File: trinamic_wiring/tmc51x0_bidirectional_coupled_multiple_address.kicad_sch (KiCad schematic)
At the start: 3 parts

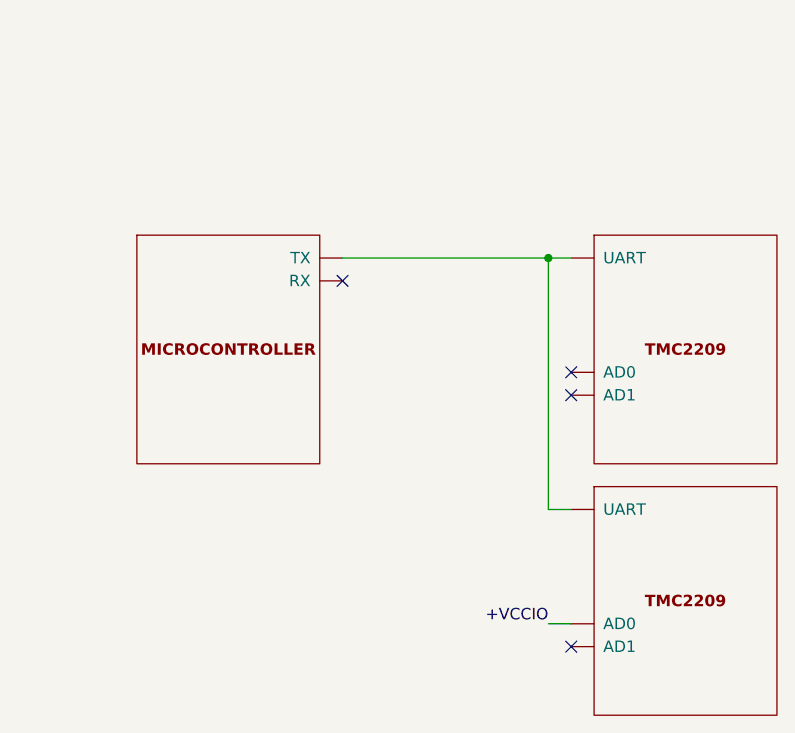
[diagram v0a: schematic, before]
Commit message: Add TMC51X0 files
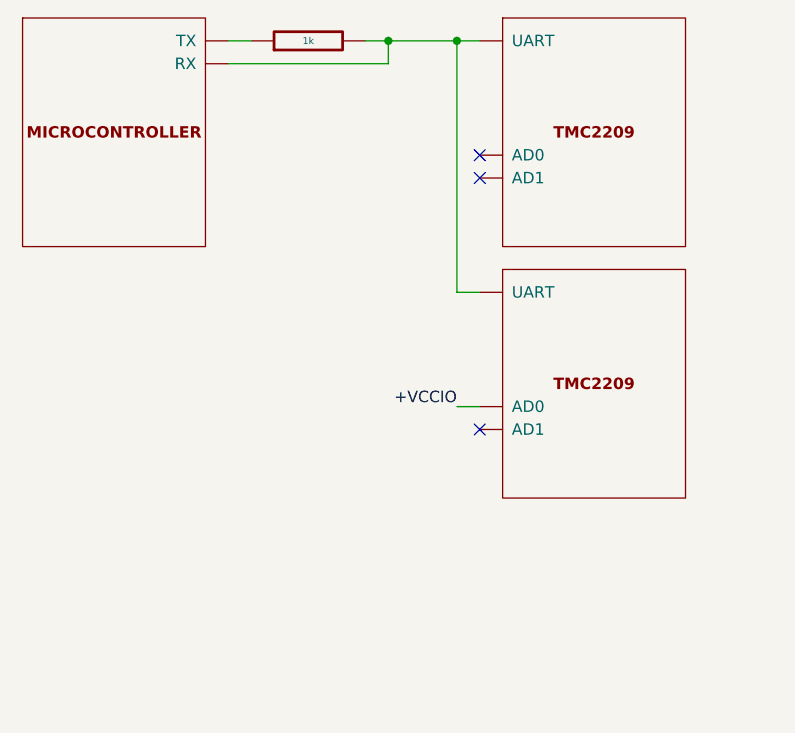
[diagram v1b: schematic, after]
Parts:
- removed MICROCONTROLLER3: DOC_MCU, symbol Janelia:DOC_MCU
- removed TMC4, TMC5: DOC_TMC2209, symbol Janelia:DOC_TMC2209
- added MICROCONTROLLER7: DOC_MCU, symbol Janelia:DOC_MCU
- added R4: 1k, Janelia:R_0402_1005Metric, symbol Janelia:R_1k_0402
- added TMC11, TMC12: DOC_TMC2209, symbol Janelia:DOC_TMC2209
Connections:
- net +VCCIO: now also TMC12.9 (AD0)
- new net: MICROCONTROLLER7.0 (RX), R4.2, TMC11.0 (UART), TMC12.0 (UART)
- new net: MICROCONTROLLER7.1 (TX), R4.1
- no-connect marks 4 -> 3
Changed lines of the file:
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@@
     (company "Janelia Research Campus")
   )
-  (junction (at 161.29 101.6) (diameter 0) (color 0 0 0 0)
+  (junction (at 151.13 77.47) (diameter 0) (color 0 0 0 0)
   )
-  (no_connect (at 163.83 116.84))
-  (no_connect (at 163.83 114.3))
-  (no_connect (at 138.43 104.14))
-  (no_connect (at 163.83 144.78))
-  (wire (pts (xy 161.29 101.6) (xy 161.29 129.54))
+  (junction (at 143.51 77.47) (diameter 0) (color 0 0 0 0)
+  )
+  (no_connect (at 153.67 120.65))
+  (no_connect (at 153.67 92.71))
+  (no_connect (at 153.67 90.17))
+  (wire (pts (xy 125.73 77.47) (xy 128.27 77.47))
     (stroke (width 0) (type default))
   )
-  (wire (pts (xy 138.43 101.6) (xy 161.29 101.6))
+  (wire (pts (xy 143.51 77.47) (xy 151.13 77.47))
     (stroke (width 0) (type default))
   )
-  (wire (pts (xy 161.29 142.24) (xy 163.83 142.24))
+  (wire (pts (xy 151.13 77.47) (xy 151.13 105.41))
     (stroke (width 0) (type default))
   )
-  (wire (pts (xy 161.29 129.54) (xy 163.83 129.54))
+  (wire (pts (xy 143.51 77.47) (xy 143.51 80.01))
     (stroke (width 0) (type default))
   )
-  (wire (pts (xy 161.29 101.6) (xy 163.83 101.6))
+  (wire (pts (xy 140.97 77.47) (xy 143.51 77.47))
     (stroke (width 0) (type default))
   )
-  (label "+VCCIO" (at 161.29 142.24 180) (fields_autoplaced)
+  (wire (pts (xy 151.13 77.47) (xy 153.67 77.47))
+    (stroke (width 0) (type default))
+  )
+  (wire (pts (xy 125.73 80.01) (xy 143.51 80.01))
+    (stroke (width 0) (type default))
+  )
+  (wire (pts (xy 151.13 105.41) (xy 153.67 105.41))
+    (stroke (width 0) (type default))
+  )
+  (wire (pts (xy 151.13 118.11) (xy 153.67 118.11))
+    (stroke (width 0) (type default))
+  )
+  (label "+VCCIO" (at 151.13 118.11 180) (fields_autoplaced)
     (effects (font (size 1.27 1.27)) (justify right bottom))
   )
-  (symbol (lib_id "Janelia:DOC_TMC2209") (at 176.53 139.7 0) (unit 1)
+  (symbol (lib_name "DOC_TMC2209_1") (lib_id "Janelia:DOC_TMC2209") (at 166.37 87.63 0) (unit 1)
     (in_bom yes) (on_board yes) (dnp no) (fields_autoplaced)
-    (property "Reference" "TMC5" (at 176.53 120.65 0)
+    (property "Reference" "TMC11" (at 166.37 68.58 0)
       (effects (font (size 1.27 1.27)) hide)
     )
-    (property "Value" "DOC_TMC2209" (at 176.53 125.73 0)
+    (property "Value" "DOC_TMC2209" (at 166.37 73.66 0)
       (effects (font (size 1.524 1.524)) hide)
     )
-    (property "Footprint" "" (at 173.99 166.37 0)
+    (property "Footprint" "" (at 163.83 114.3 0)
       (effects (font (size 1.524 1.524)) hide)
     )
-    (property "Datasheet" "" (at 176.53 139.7 0)
+    (property "Datasheet" "" (at 166.37 87.63 0)
       (effects (font (size 1.524 1.524)) hide)
     )
-    (property "Sim.Enable" "0" (at 176.53 123.19 0)
+    (property "Sim.Enable" "0" (at 166.37 71.12 0)
       (effects (font (size 1.27 1.27)) hide)
     )
@@
     (instances
       (project "trinamic_wiring"
-        (path "/e4144788-6304-493f-818e-5d881d3b7418/c8eda2b5-ab13-4033-82d9-875c9fcaf884/a2ce530e-f5b5-4e3e-9188-e4bc8f84c739"
-          (reference "TMC5") (unit 1)
+        (path "/e4144788-6304-493f-818e-5d881d3b7418/c8eda2b5-ab13-4033-82d9-875c9fcaf884/5f6f310d-167d-42a3-8815-1b623fe73dc8"
+          (reference "TMC11") (unit 1)
         )
-        (path "/e4144788-6304-493f-818e-5d881d3b7418/a161638e-a96f-4455-865a-1d7502675f43/a2ce530e-f5b5-4e3e-9188-e4bc8f84c739"
-          (reference "TMC6") (unit 1)
+        (path "/e4144788-6304-493f-818e-5d881d3b7418/a161638e-a96f-4455-865a-1d7502675f43/5f6f310d-167d-42a3-8815-1b623fe73dc8"
+          (reference "TMC11") (unit 1)
         )
       )
     )
   )
-  (symbol (lib_name "DOC_TMC2209_1") (lib_id "Janelia:DOC_TMC2209") (at 176.53 111.76 0) (unit 1)
+  (symbol (lib_id "Janelia:DOC_TMC2209") (at 166.37 115.57 0) (unit 1)
     (in_bom yes) (on_board yes) (dnp no) (fields_autoplaced)
-    (property "Reference" "TMC4" (at 176.53 92.71 0)
+    (property "Reference" "TMC12" (at 166.37 96.52 0)
       (effects (font (size 1.27 1.27)) hide)
     )
-    (property "Value" "DOC_TMC2209" (at 176.53 97.79 0)
+    (property "Value" "DOC_TMC2209" (at 166.37 101.6 0)
       (effects (font (size 1.524 1.524)) hide)
     )
-    (property "Footprint" "" (at 173.99 138.43 0)
+    (property "Footprint" "" (at 163.83 142.24 0)
       (effects (font (size 1.524 1.524)) hide)
     )
-    (property "Datasheet" "" (at 176.53 111.76 0)
+    (property "Datasheet" "" (at 166.37 115.57 0)
       (effects (font (size 1.524 1.524)) hide)
     )
-    (property "Sim.Enable" "0" (at 176.53 95.25 0)
+    (property "Sim.Enable" "0" (at 166.37 99.06 0)
       (effects (font (size 1.27 1.27)) hide)
     )
@@
     (instances
       (project "trinamic_wiring"
-        (path "/e4144788-6304-493f-818e-5d881d3b7418/c8eda2b5-ab13-4033-82d9-875c9fcaf884/a2ce530e-f5b5-4e3e-9188-e4bc8f84c739"
-          (reference "TMC4") (unit 1)
+        (path "/e4144788-6304-493f-818e-5d881d3b7418/c8eda2b5-ab13-4033-82d9-875c9fcaf884/5f6f310d-167d-42a3-8815-1b623fe73dc8"
+          (reference "TMC12") (unit 1)
         )
-        (path "/e4144788-6304-493f-818e-5d881d3b7418/a161638e-a96f-4455-865a-1d7502675f43/a2ce530e-f5b5-4e3e-9188-e4bc8f84c739"
-          (reference "TMC6") (unit 1)
+        (path "/e4144788-6304-493f-818e-5d881d3b7418/a161638e-a96f-4455-865a-1d7502675f43/5f6f310d-167d-42a3-8815-1b623fe73dc8"
+          (reference "TMC12") (unit 1)
         )
       )
     )
   )
-  (symbol (lib_id "Janelia:DOC_MCU") (at 125.73 111.76 0) (unit 1)
-    (in_bom yes) (on_board yes) (dnp no) (fields_autoplaced)
-    (property "Reference" "MICROCONTROLLER3" (at 125.73 92.71 0)
+  (symbol (lib_id "Janelia:R_1k_0402") (at 134.62 77.47 90) (unit 1)
+    (in_bom yes) (on_board yes) (dnp no)
+    (property "Reference" "R4" (at 134.62 76.2 0)
+      (effects (font (size 1.016 1.016)) (justify left) hide)
+    )
+    (property "Value" "1k" (at 134.62 77.47 90)
+      (effects (font (size 0.762 0.762)))
+    )
+    (property "Footprint" "Janelia:R_0402_1005Metric" (at 134.62 79.248 90)
+      (effects (font (size 0.762 0.762)) hide)
+    )
+    (property "Datasheet" "" (at 134.62 75.438 90)
+      (effects (font (size 0.762 0.762)))
+    )
+    (property "Vendor" "Digi-Key" (at 132.08 72.898 90)
+      (effects (font (size 1.524 1.524)) hide)
+    )
+    (property "Vendor Part Number" "311-1.00KLRCT-ND" (at 129.54 70.358 90)
+      (effects (font (size 1.524 1.524)) hide)
+    )
+    (property "Description" "RES SMD 1K OHM 1% 1/16W" (at 127 67.818 90)
+      (effects (font (size 1.524 1.524)) hide)
+    )
+    (property "Package" "0402" (at 134.62 77.47 0)
       (effects (font (size 1.27 1.27)) hide)
     )
-    (property "Value" "DOC_MCU" (at 125.73 97.79 0)
+    (property "Manufacturer" "YAGEO" (at 134.62 77.47 0)
+      (effects (font (size 1.27 1.27)) hide)
+    )
+    (property "Manufacturer Part Number" "RC0402FR-071KL" (at 134.62 77.47 0)
+      (effects (font (size 1.27 1.27)) hide)
+    )
+    (pin "1")
+    (pin "2")
+    (instances
+      (project "trinamic_wiring"
+        (path "/e4144788-6304-493f-818e-5d881d3b7418/c8eda2b5-ab13-4033-82d9-875c9fcaf884/5f6f310d-167d-42a3-8815-1b623fe73dc8"
+          (reference "R4") (unit 1)
+        )
+        (path "/e4144788-6304-493f-818e-5d881d3b7418/a161638e-a96f-4455-865a-1d7502675f43/5f6f310d-167d-42a3-8815-1b623fe73dc8"
+          (reference "R4") (unit 1)
+        )
+      )
+    )
+  )
+  (symbol (lib_id "Janelia:DOC_MCU") (at 113.03 87.63 0) (unit 1)
+    (in_bom yes) (on_board yes) (dnp no) (fields_autoplaced)
+    (property "Reference" "MICROCONTROLLER7" (at 113.03 68.58 0)
+      (effects (font (size 1.27 1.27)) hide)
+    )
+    (property "Value" "DOC_MCU" (at 113.03 73.66 0)
       (effects (font (size 1.524 1.524)) hide)
     )
-    (property "Footprint" "" (at 123.19 138.43 0)
+    (property "Footprint" "" (at 110.49 114.3 0)
       (effects (font (size 1.524 1.524)) hide)
     )
-    (property "Datasheet" "" (at 125.73 111.76 0)
+    (property "Datasheet" "" (at 113.03 87.63 0)
       (effects (font (size 1.524 1.524)) hide)
     )
-    (property "Sim.Enable" "0" (at 125.73 95.25 0)
+    (property "Sim.Enable" "0" (at 113.03 71.12 0)
       (effects (font (size 1.27 1.27)) hide)
     )
@@
     (instances
       (project "trinamic_wiring"
-        (path "/e4144788-6304-493f-818e-5d881d3b7418/c8eda2b5-ab13-4033-82d9-875c9fcaf884/a2ce530e-f5b5-4e3e-9188-e4bc8f84c739"
-          (reference "MICROCONTROLLER3") (unit 1)
+        (path "/e4144788-6304-493f-818e-5d881d3b7418/c8eda2b5-ab13-4033-82d9-875c9fcaf884/5f6f310d-167d-42a3-8815-1b623fe73dc8"
+          (reference "MICROCONTROLLER7") (unit 1)
         )
-        (path "/e4144788-6304-493f-818e-5d881d3b7418/a161638e-a96f-4455-865a-1d7502675f43/a2ce530e-f5b5-4e3e-9188-e4bc8f84c739"
-          (reference "MICROCONTROLLER4") (unit 1)
+        (path "/e4144788-6304-493f-818e-5d881d3b7418/a161638e-a96f-4455-865a-1d7502675f43/5f6f310d-167d-42a3-8815-1b623fe73dc8"
+          (reference "MICROCONTROLLER7") (unit 1)
         )
       )
